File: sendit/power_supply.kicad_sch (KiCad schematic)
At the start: 36 parts, among them U7 TPS7A2033PDBVR, U8 TPS61040DBV, U9 REF35330QDBVR

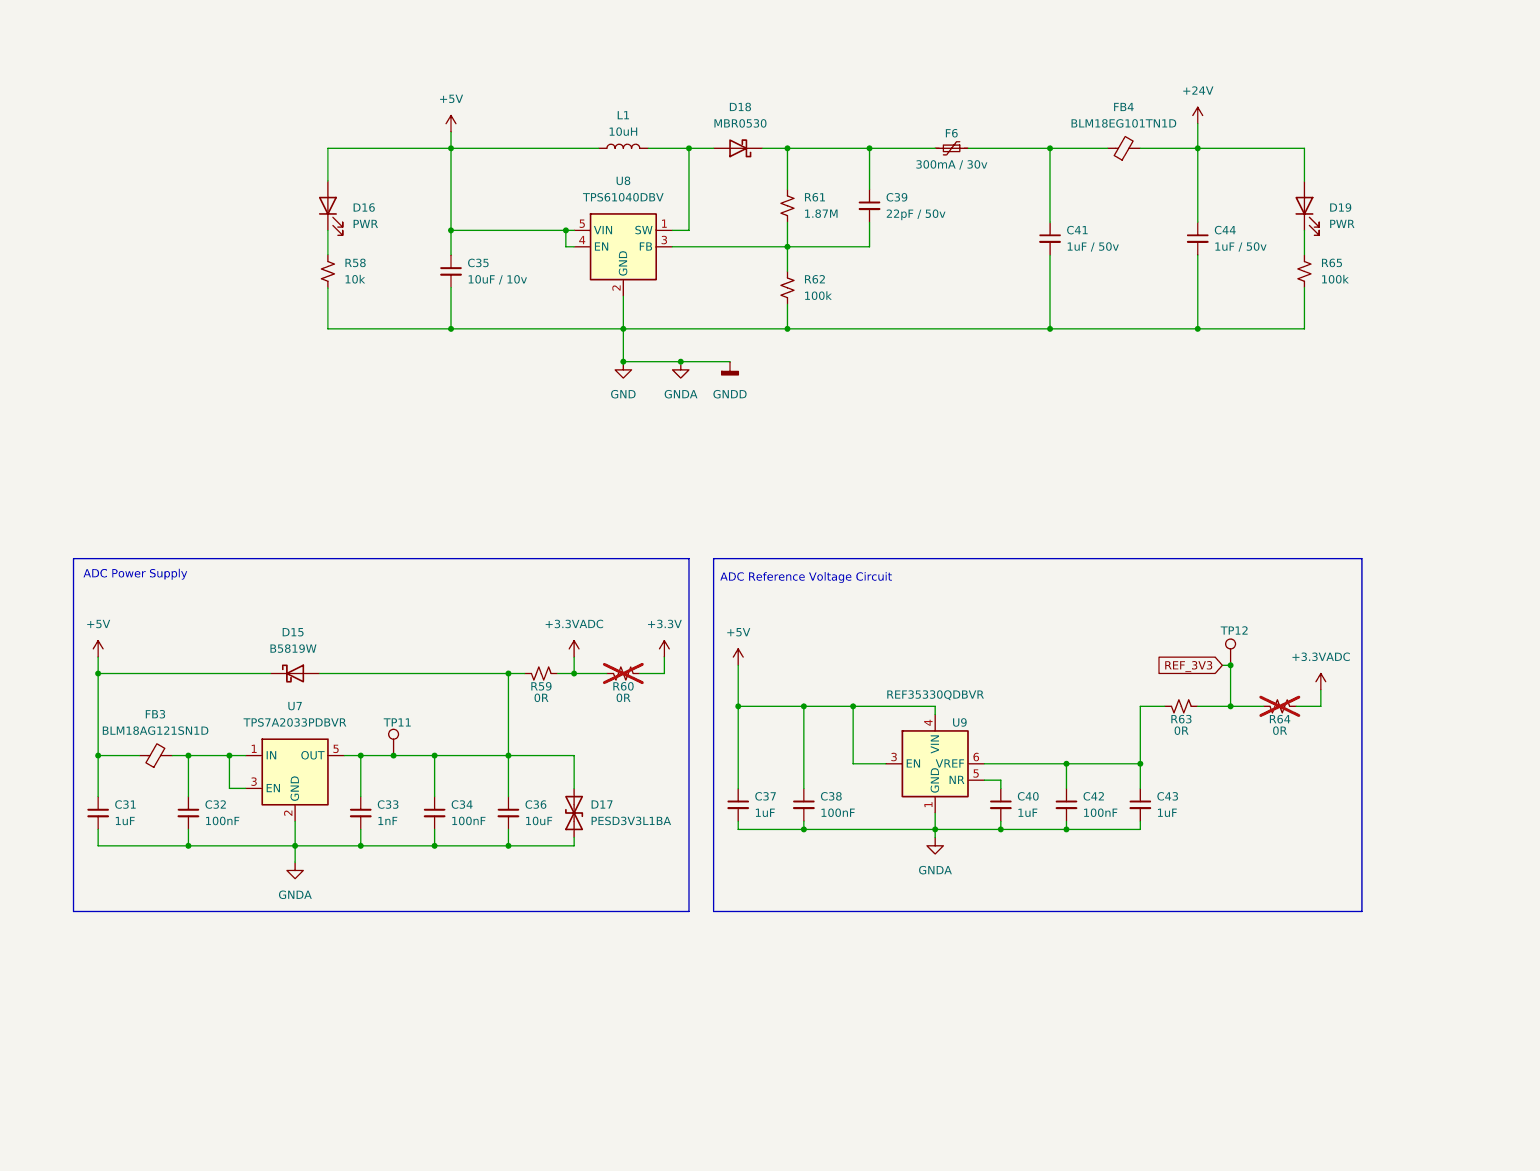
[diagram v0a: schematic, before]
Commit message: passing erc and drc
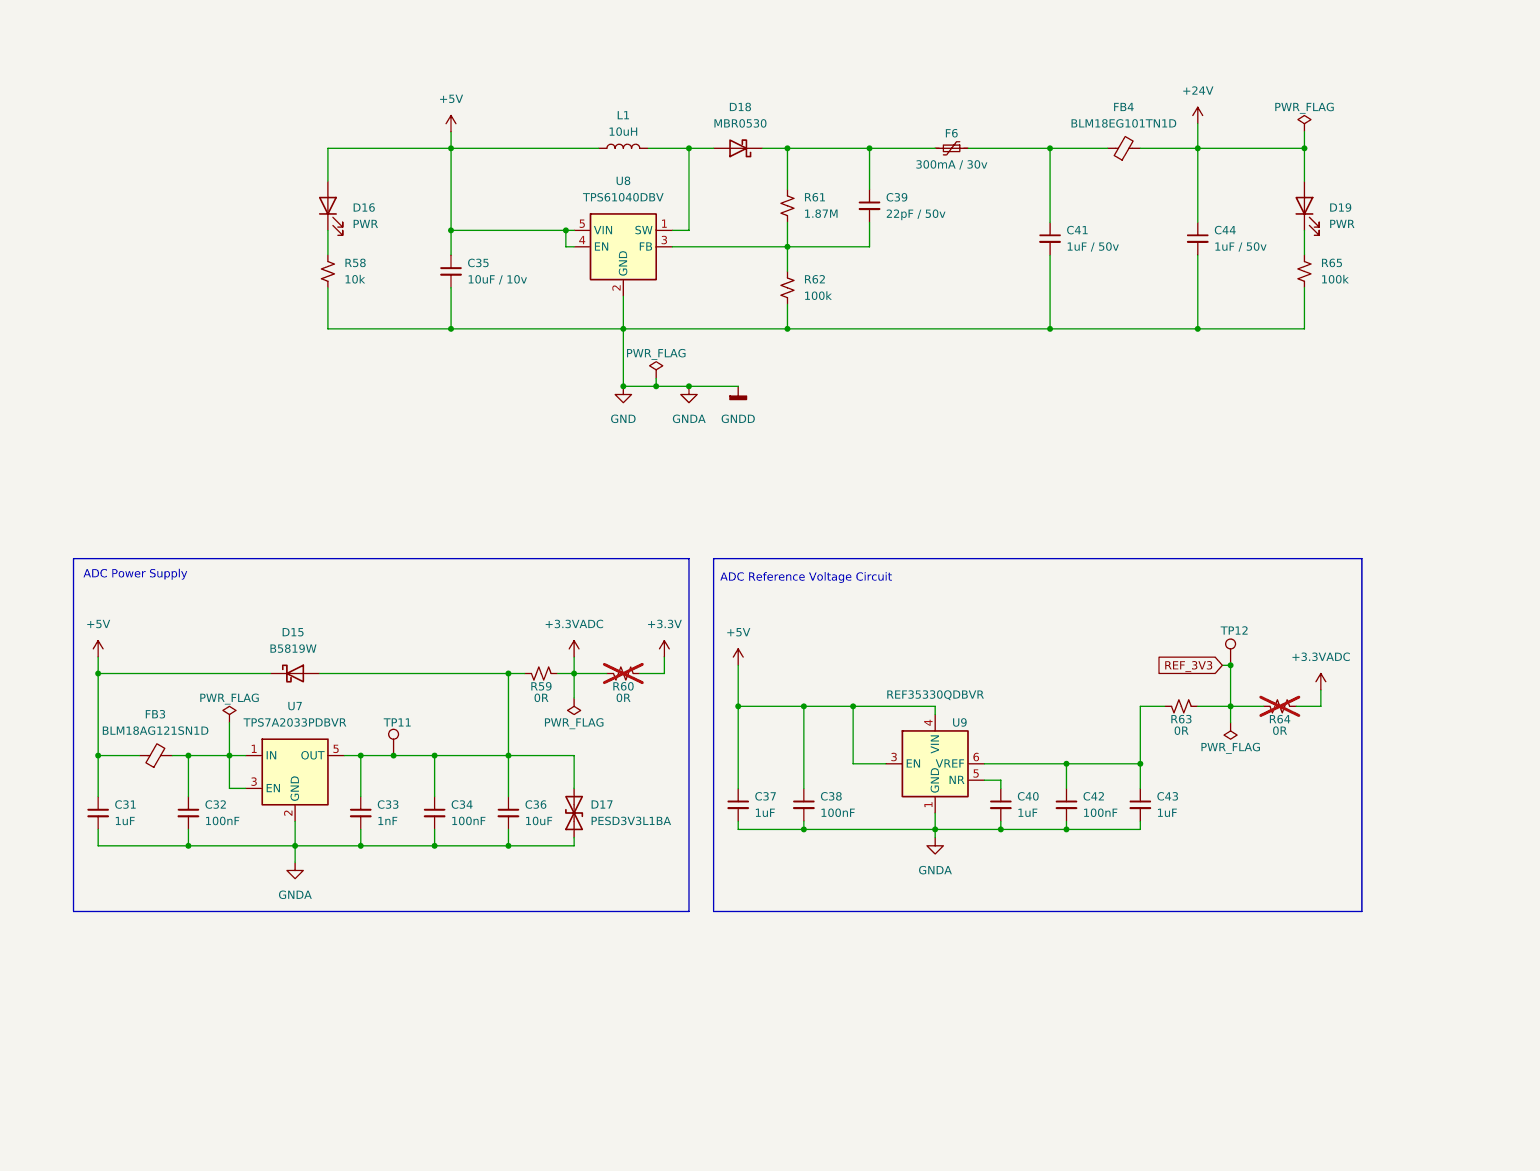
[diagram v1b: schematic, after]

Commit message: bom and placement looking good.
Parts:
- D16, D19: value PWR -> RED
- D17: value PESD3V3L1BA -> PESD3V3L1BA,115
- FB3: LCSC (none) -> C76893
- FB4: value BLM18EG101TN1D -> BLM18AG121SN1D
- U8, U9: Rotation Offset (none) -> 90

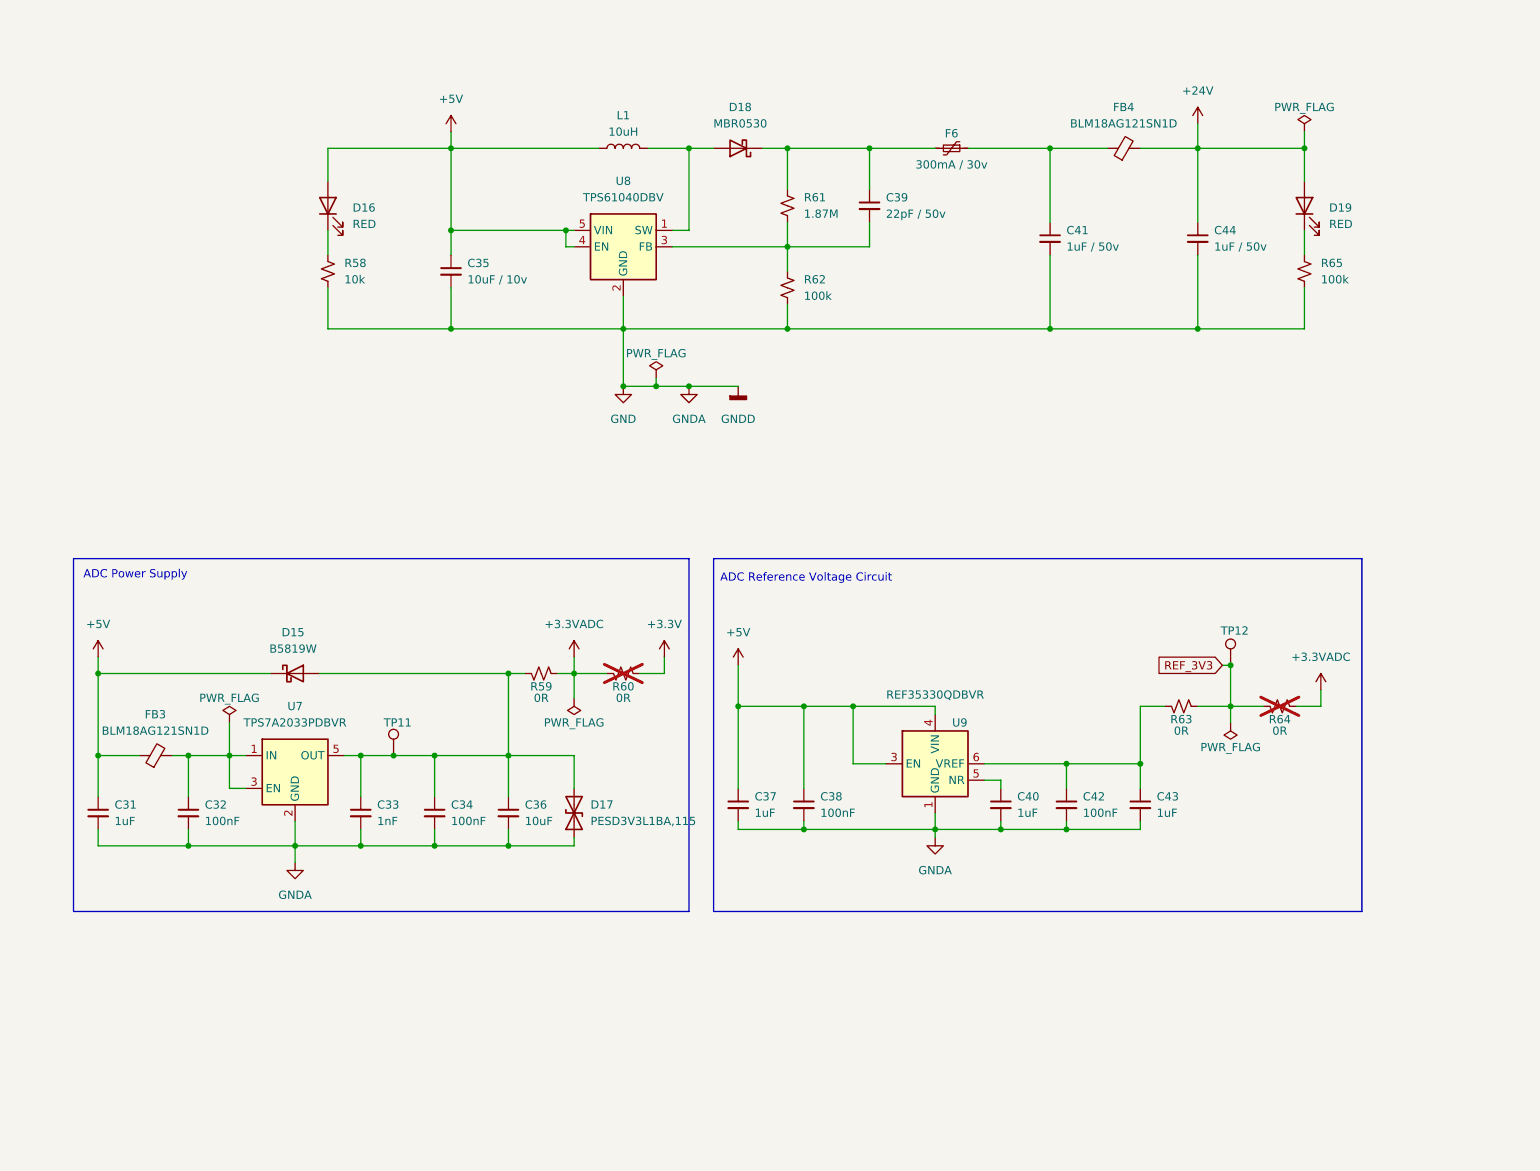
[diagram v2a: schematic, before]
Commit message: cleaning up schematics a bit for design review
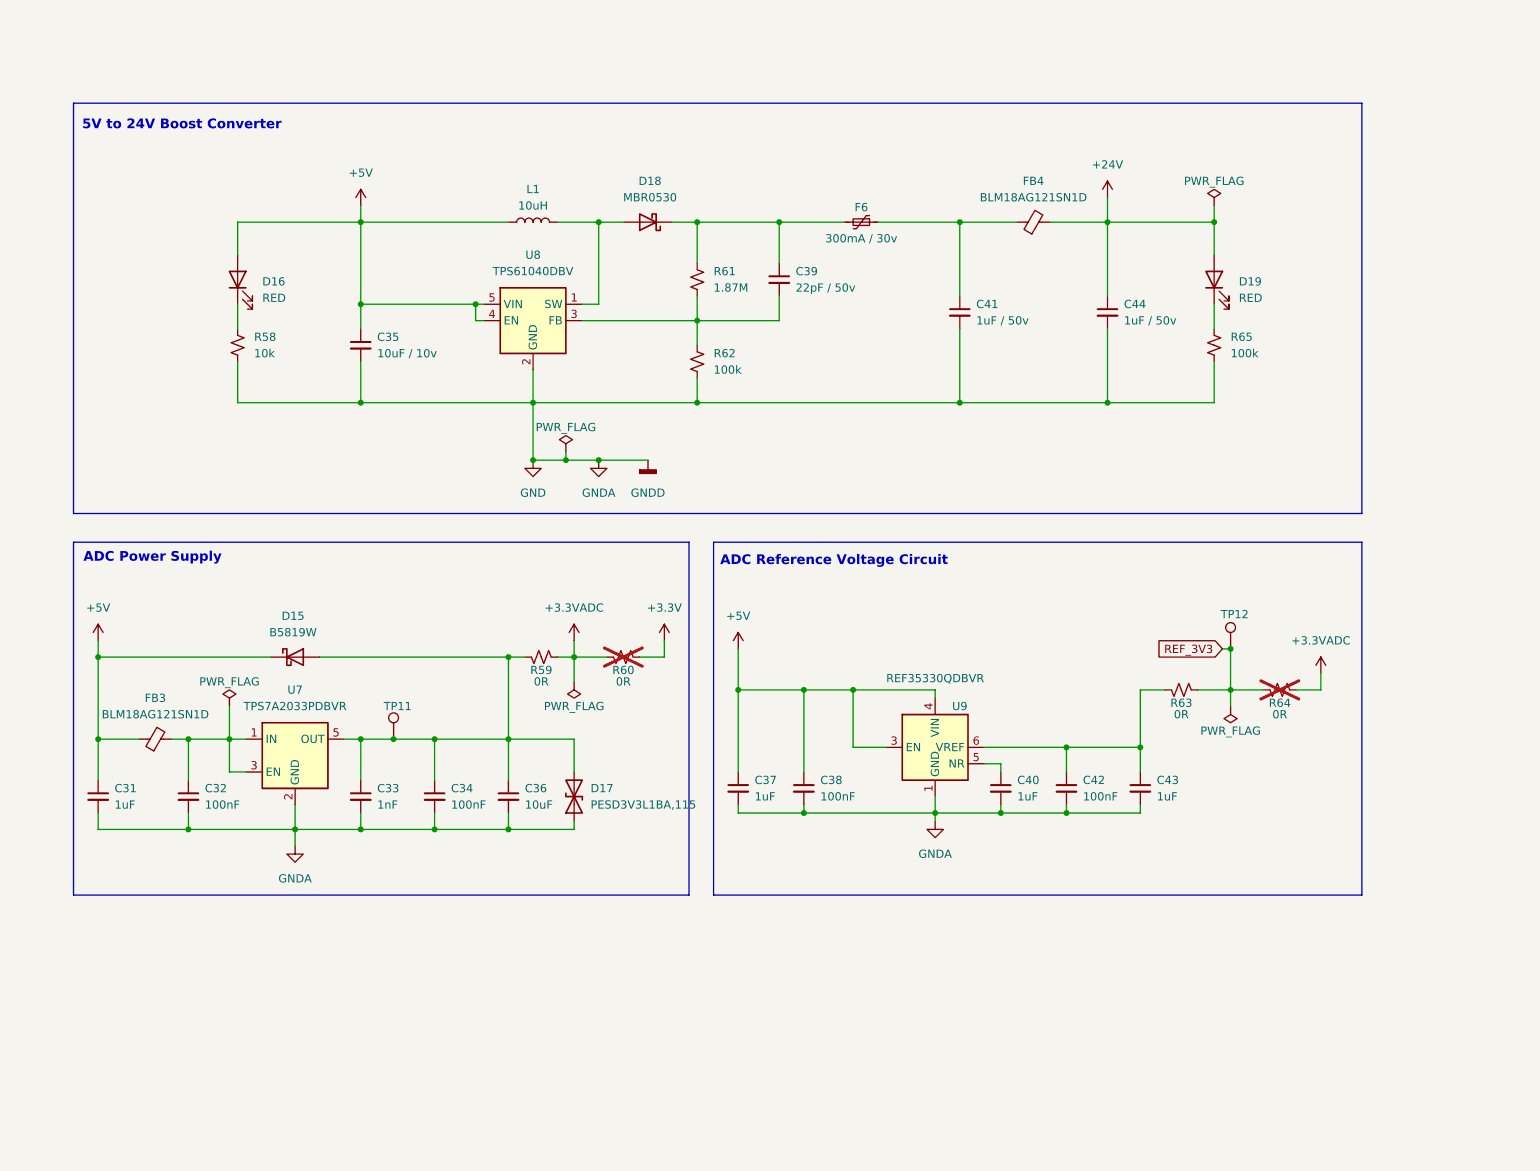
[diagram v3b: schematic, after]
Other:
- note added: "5V to 24V Boost Converter"
- title: (none) -> https://github.com/hoeken/sendit
- moved on the sheet: C31, C32, C33, C34, C35, C36, C37, C38, C39, C40, C41, C42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

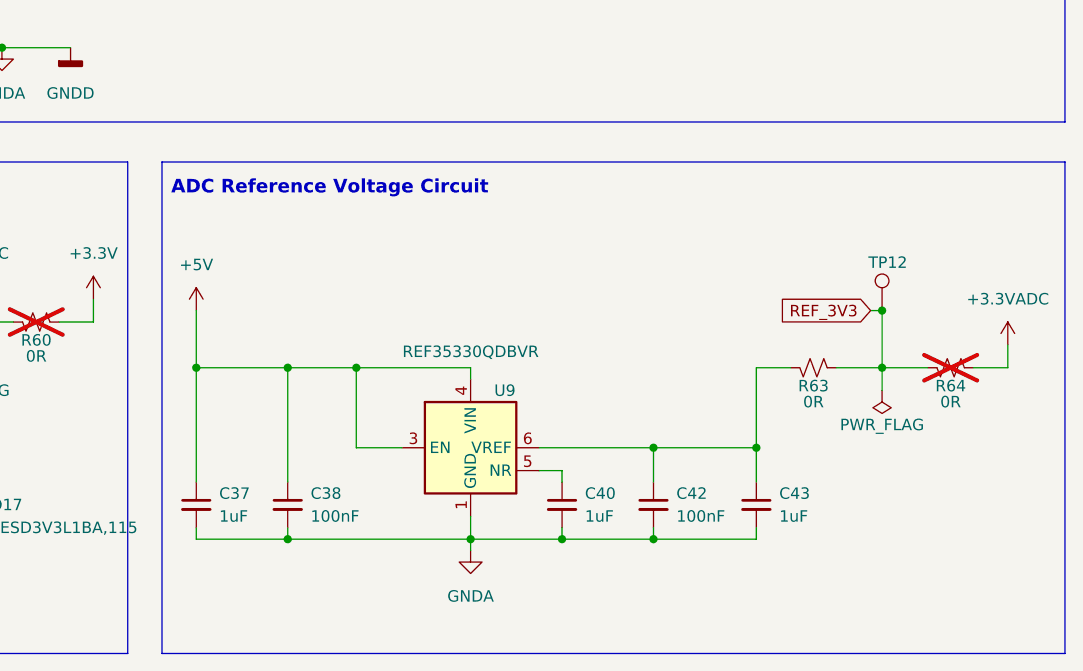
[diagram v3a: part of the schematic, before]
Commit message: started work on the rev c schematic
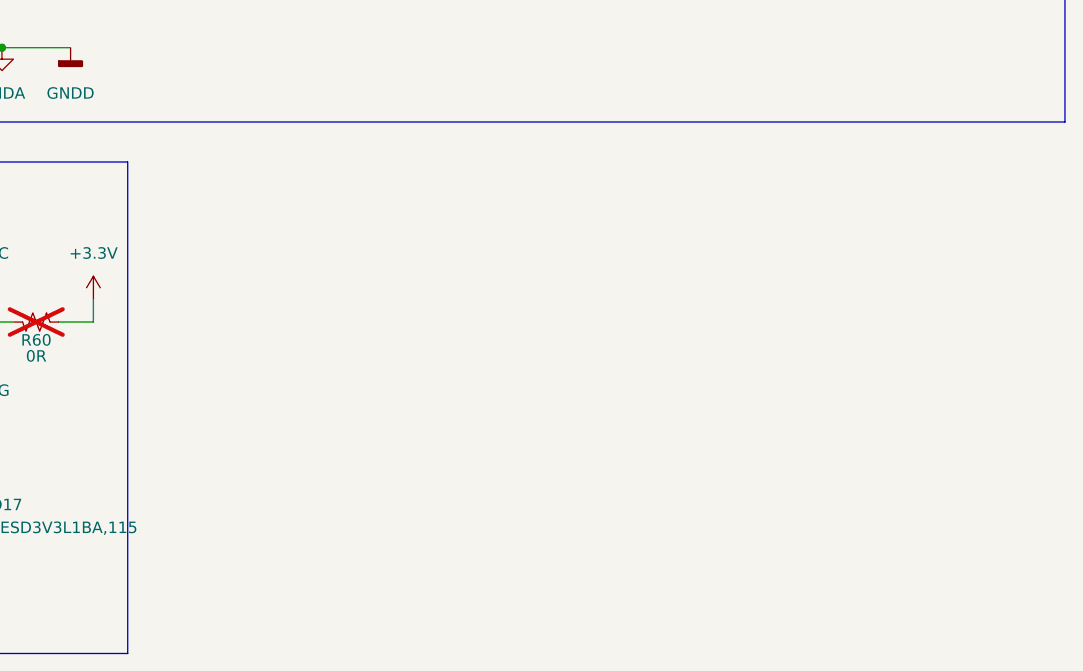
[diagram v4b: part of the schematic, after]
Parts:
- removed C37, C40, C43: 1uF, Capacitor_SMD:C_0603_1608Metric, symbol Device:C_Small
- removed C38, C42: 100nF, Capacitor_SMD:C_0603_1608Metric, symbol Device:C_Small
- removed R63, R64: 0R, Resistor_SMD:R_0603_1608Metric, symbol Device:R_Small_US
- removed TP12: TestPoint, TestPoint:TestPoint_THTPad_D2.0mm_Drill1.0mm, symbol Connector:TestPoint
- removed U9: REF35330QDBVR, Package_TO_SOT_SMD:SOT-23-6, symbol Reference_Voltage:REF35330QDBVR
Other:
- note removed: "ADC Reference Voltage Circuit"

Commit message: more work on rev c board schematic
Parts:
- added C14: 10uF, Capacitor_SMD:C_0805_2012Metric, symbol Device:C_Small
- added C25: 100nF, Capacitor_SMD:C_0603_1608Metric, symbol Device:C_Small
- added C37, C38: 22uF, Capacitor_SMD:C_0603_1608Metric, symbol Device:C_Small
- added D14: GREEN, LED_SMD:LED_0603_1608Metric, symbol Device:LED
- added F10: 300mA / 30v, Fuse:Fuse_0805_2012Metric, symbol Device:Polyfuse_Small
- added J58: JUMPER, symbol Connector_Generic:Conn_01x02
- added J59: Conn_01x02, Connector_PinSocket_2.54mm:PinSocket_1x02_P2.54mm_Vertical, symbol Connector_Generic:Conn_01x02
- added L2: 4.7 uH, Inductor_SMD:CKCS3010, symbol Device:L
- added R23: 100k, Resistor_SMD:R_0603_1608Metric, symbol Device:R_Small_US
- added TP12, TP19, TP23, TP24: ~, TestPoint:TestPoint_THTPad_D2.0mm_Drill1.0mm, symbol Connector:TestPoint
- added U11: AP63205WU, Package_TO_SOT_SMD:TSOT-26, symbol Regulator_Switching:AP63205WU
- D16, D19: value RED -> GREEN
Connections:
- net +24V: now also TP19.1
- net +5V: now also C37.1, C38.1, L2.2, TP12.1, U11.1 (FB)
- net GND: now also C14.2, C37.2, C38.2, R23.2, TP23.1, U11.4 (GND)
- new net: D14.1 (K), R23.1
- new net: F10.1, J59.2 (Pin_2)
- new net: C14.1, F10.2, TP24.1, U11.2 (EN), U11.3 (IN)
- new net VEXT: D14.2 (A), J59.1 (Pin_1)
- new net bst: C25.2, U11.6 (BST)
- new net sw_node: C25.1, L2.1, U11.5 (SW)
- no-connect marks 0 -> 2
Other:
- note added: "24v to 5v Converter"
- moved on the sheet: C35, C39, C41, C44, D16, D18, D19, F6, FB4, L1, R58, R61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

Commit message: most of the work on the schematic is done.
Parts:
- removed D15: B5819W, Diode_SMD:D_SOD-123, symbol Device:D_Schottky
- added D16, D20: MBR0530, Diode_SMD:D_SOD-123, symbol Diode:MBR0530
- added INPUT1: Conn_01x02, yarrboard:PhoenixContact_MC_1,5_2-G-3.5_1x02_P3.50mm_Horizontal, symbol Connector_Generic:Conn_01x02
- added J1: Conn_01x02, symbol Connector_Generic:Conn_01x02
- L2: footprint Inductor_SMD:CKCS3010 -> Inductor_SMD:L_Neosid_SMS-ME3010
- U11: footprint Package_TO_SOT_SMD:TSOT-26 -> Package_TO_SOT_SMD:TSOT-23-6
- renumbered C31 to C28, C32 to C29, C33 to C30, C35 to C31, C34 to C32, C36 to C33, C39 to C34, C41 to C35, C14 to C36, C44 to C37, C25 to C38, C37 to C39, C38 to C40, D16 to D15, D14 to D19, D19 to D21, F10 to F7, FB3 to FB2, FB4 to FB3, J59 to J37, J58 to J38, R58 to R53, R59 to R54, R60 to R55, R61 to R56, R62 to R57, R23 to R58, R65 to R59, TP12 to TP14, TP11 to TP15, TP23 to TP16, TP24 to TP17, TP19 to TP18, U8 to U10, U7 to U9
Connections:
- net +5V: now also D16.1 (K)
- net GND: now also INPUT1.2 (Pin_2)
- net VEXT: now also D20.1 (K)
- net at C30.1, C32.1, C33.1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: now also D16.2 (A)
- new net: D20.2 (A), INPUT1.1 (Pin_1)
- no-connect marks 2 -> 4
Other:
- note added: "24v to 5v Buck Converter"
- note added: "External Voltage Input"
- note added: "FEMALE"
- note added: "MALE"
- note removed: "24v to 5v Converter"
- moved on the sheet: C28, C29, C30, C31, C32, C33, C34, C35, C36, C37, C38, C39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

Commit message: more work towards rev c board.
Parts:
- removed R54, R55: 0R, Resistor_SMD:R_0603_1608Metric, symbol Device:R_Small_US
- added JP1: SolderJumper_3_Bridged12, Jumper:SolderJumper-3_P1.3mm_Bridged12_RoundedPad1.0x1.5mm, symbol Jumper:SolderJumper_3_Bridged12
- TP14, TP15, TP16, TP17, TP18: footprint TestPoint:TestPoint_THTPad_D2.0mm_Drill1.0mm -> TestPoint:TestPoint_THTPad_D1.5mm_Drill0.7mm
- renumbered C31 to C30, C30 to C31, C36 to C34, C34 to C35, C35 to C36, C38 to C37, C37 to C38, D20 to D16, D16 to D17, D19 to D18, D18 to D19, D17 to D20, F7 to F6, F6 to F7, INPUT1 to INPUT6, J1 to J36, R53 to R51, R58 to R52, R56 to R53, R57 to R54, R59 to R55
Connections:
- net +3.3V: now also JP1.1 (A)
- net +3.3VADC: now also JP1.2 (C)
- net at C31.1, C32.1, C33.1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: now also JP1.3 (B)

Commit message: more rev c progress
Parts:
- C34: value 10uF -> 10uF / 50v; footprint Capacitor_SMD:C_0805_2012Metric -> Capacitor_SMD:C_0603_1608Metric; LCSC C440198 -> (none); PARTNUM GRM21BR61H106KE43L -> (none)
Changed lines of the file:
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@@
 			)
 		)
-		(property "Value" "10uF"
+		(property "Value" "10uF / 50v"
 			(at 121.92 118.1162 0)
 			(effects
@@
 			)
 		)
-		(property "Footprint" "Capacitor_SMD:C_0805_2012Metric"
+		(property "Footprint" "Capacitor_SMD:C_0603_1608Metric"
 			(at 119.38 116.84 0)
 			(effects
@@
 			)
 		)
-		(property "LCSC" "C440198"
+		(property "LCSC" ""
 			(at 119.38 116.84 0)
 			(effects
-				(font
-					(size 1.27 1.27)
-				)
-				(hide yes)
-			)
-		)
-		(property "PARTNUM" "GRM21BR61H106KE43L"
-			(at 119.38 116.84 0)
-			(effects
